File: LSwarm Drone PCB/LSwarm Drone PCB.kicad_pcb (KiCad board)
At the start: 4 copper layers, 100 x 99.8 mm, 135 parts, among them J1 Conn_01x04_Pin, J3 JST / BT2.0 Connector, J4 Conn_01x02_Pin, J5 Conn_01x02_Pin, J6 Conn_01x02_Pin, J7 Conn_01x02_Pin, Q1 AO3400A, Q2 AO3400A, Q3 AO3400A, Q4 AO3400A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

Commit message: sync
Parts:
- moved C59 2.50 mm to (54.5, 41.5)
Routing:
- net +3.3V: track 227.7 -> 230.4 mm
- net BATT_SW+: track 346.7 -> 344.4 mm

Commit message: sync
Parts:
- L6: value L -> 24nH
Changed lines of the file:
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@@
 		(capping no)
 		(filling no)
-		(zone_defaults)
 		(pcbplotparams
 			(layerselection 0x00000000_00000000_55555555_5755f5ff)
@@
 			)
 		)
-		(property "Value" "L"
+		(property "Value" "24nH"
 			(at 0 1.55 0)
 			(layer "F.Fab")

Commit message: sync
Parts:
- removed C52, C55: 12pF, Capacitor_SMD:C_0603_1608Metric
- removed C72: 220uF, Capacitor_Tantalum_SMD:CP_EIA-3528-21_Kemet-B
- removed L6: 24nH, Inductor_SMD:L_0805_2012Metric
- removed R18: 110k, Resistor_SMD:R_0603_1608Metric
- removed Y1: 12MHz, Crystal:Crystal_SMD_3225-4Pin_3.2x2.5mm
- removed Y3: 40MHz, Crystal:Crystal_SMD_3225-4Pin_3.2x2.5mm
- added C1: CL21A226MAQNNNE, easyeda2kicad:C0805, F.Cu at (54.0, 68.5)
- added R36: 820k, Resistor_SMD:R_0603_1608Metric, F.Cu at (62.5, 56.0)
- added R37: 100k, Resistor_SMD:R_0603_1608Metric, F.Cu at (66.0, 56.5)
- added X1: X322512MSB4SI, easyeda2kicad:CRYSTAL-SMD_4P-L3.2-W2.5-BL, F.Cu at (54.8, 52.3)
- R17: value 806k -> 10k
- moved R17 18.0 mm to (62.5, 74.0), turned to 0 degrees
- moved C7 4.72 mm to (56.5, 49.0), turned to -90 degrees
- moved C60 4.17 mm to (70.8, 40.0)
- moved C61 4.17 mm to (73.5, 36.5)
- moved L8 4.17 mm to (71.0, 38.5)
- moved JP1 3.76 mm to (73.5, 45.2)
- moved C8 1.11 mm to (55.0, 49.0), turned to -90 degrees
- renumbered C71C to C71Ceramic1
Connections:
- C7 pad 1: Net-(C7-Pad1) -> GND
- C7 pad 2: GND -> Net-(X1-OSC2)
- C8 pad 1: RP2350_XIN -> GND
- C8 pad 2: GND -> RP2350_XIN
- R17 pad 1: Net-(U3-FB) -> Net-(R17-Pad1)
- R17 pad 2: +5V -> Net-(Q7-G)
- R7 pad 1: Net-(C7-Pad1) -> Net-(X1-OSC2)
- SW1 pad 2: Net-(Q7-G) -> Net-(R17-Pad1)
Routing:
- net Net-(R17-Pad1): track 0.00 -> 51.4 mm, vias 0 -> 2
- net Net-(Q7-G): track 56.0 -> 9.82 mm, vias 3 -> 2
- net Net-(C7-Pad1): track 13.3 -> 0.00 mm, vias 2 -> 0
- net ESP32_40M_X0: track 12.4 -> 0.00 mm, vias 4 -> 0
- net Net-(C52-Pad1): track 10.1 -> 0.00 mm, vias 2 -> 0
- net Net-(ESP32-LNA_IN): track 22.9 -> 13.0 mm
- net Net-(X1-OSC2): track 0.00 -> 9.14 mm, vias 0 -> 2
- net ESP32_40M_X1: track 6.14 -> 0.00 mm
- net RP2350_XIN: track 20.7 -> 17.5 mm
- net GND: track 123.0 -> 125.4 mm, vias 102 -> 100
- net BATT_SW+: track 344.4 -> 342.4 mm
- net RP2350_GPIO_17: track 41.9 -> 40.2 mm
- net RP2350_GPIO_16: track 43.6 -> 42.8 mm
- net BATT+: track 16.3 -> 17.0 mm

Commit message: sync
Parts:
- added D5: USBLC6-2SC6_C2687116, easyeda2kicad:SOT-23-6_L2.9-W1.6-P0.95-LS2.8-BL, F.Cu at (50.0, 31.4)
- moved R32 12.5 mm to (56.5, 28.5)
- moved R33 10.5 mm to (46.0, 29.0)
- moved C60 7.32 mm to (63.5, 40.7), turned to 90 degrees
- moved C61 7.31 mm to (67.1, 40.0), turned to 90 degrees
- moved L8 6.23 mm to (65.3, 41.0)
- moved JP1 6.15 mm to (69.5, 40.6), turned to -90 degrees
- moved R35 5.49 mm to (45.2, 31.3), turned to 90 degrees
- moved R34 4.92 mm to (56.5, 30.5)
- moved C20 4.50 mm to (36.0, 59.7)
- moved C19 4.50 mm to (36.0, 56.5)
- moved C56 4.27 mm to (54.7, 41.0)
- moved C18 3.48 mm to (38.0, 56.5)
- moved C21 3.48 mm to (38.0, 59.7)
- moved C59 3.16 mm to (53.5, 44.5)
- moved C26 2.50 mm to (43.0, 25.0)
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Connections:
- R34 pad 1: Net-(USB1-DN1) -> Net-(D5-I/O2-Pad3)
- R35 pad 2: Net-(USB1-DP1) -> Net-(D5-I/O2-Pad4)
- USB1 pad A4: unconnected-(USB1-VBUS-PadA4) -> Net-(D5-VBUS)
- USB1 pad A9: unconnected-(USB1-VBUS-PadA4) -> Net-(D5-VBUS)
- USB1 pad B4: unconnected-(USB1-VBUS-PadA4) -> Net-(D5-VBUS)
- USB1 pad B9: unconnected-(USB1-VBUS-PadA4) -> Net-(D5-VBUS)
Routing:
- net Net-(D5-VBUS): track 0.00 -> 11.2 mm, vias 0 -> 2
- net RP2350_GPIO_22: track 36.8 -> 47.4 mm, vias 2 -> 4
- net Net-(USB1-DP1): track 16.8 -> 8.43 mm
- net Net-(JP1-SIG): track 10.8 -> 3.16 mm
- net Net-(USB1-DN1): track 15.3 -> 7.64 mm
- net RP2350_USB_DP: track 25.3 -> 17.8 mm
- net Net-(ESP32-LNA_IN): track 13.0 -> 5.46 mm
- net RP2350_GPIO_12: track 62.5 -> 55.7 mm, vias 7 -> 6
- net unconnected-(USB1-VBUS-PadA4): track 6.68 -> 0.00 mm
- net RP2350_USB_DM: track 27.5 -> 21.5 mm
- net GND: track 125.4 -> 131.2 mm, vias 100 -> 98
- net RP2350_GPIO_13: track 60.9 -> 55.2 mm, vias 5 -> 4
- net Net-(USB1-CC1): track 10.7 -> 6.16 mm, vias 2 -> 0
- net Net-(D5-I/O2-Pad3): track 0.00 -> 4.54 mm
- net Net-(RP2350-RUN): track 37.2 -> 32.9 mm
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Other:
- outline, holes or cut-outs redrawn

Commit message: sync
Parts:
- moved R34 3.89 mm to (52.8, 31.5), turned to -90 degrees
- moved R6 3.89 mm to (46.0, 36.1)
- moved R35 2.02 mm to (47.2, 31.7)
- turned C6 to 0 degrees
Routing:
- net RP2350_USB_DM: track 21.5 -> 16.9 mm, vias 2 -> 0
- net Net-(D5-I/O2-Pad3): track 4.54 -> 1.71 mm
- net Net-(RP2350-VREG_AVDD): track 24.7 -> 22.1 mm, vias 0 -> 2
- net +1V1: track 63.3 -> 61.4 mm
- net RP2350_USB_DP: track 17.8 -> 15.9 mm, vias 2 -> 0
- net Net-(D5-I/O2-Pad4): track 3.66 -> 1.85 mm
- net GND: track 131.2 -> 130.3 mm
- net +3.3V: track 232.9 -> 233.5 mm, vias 24 -> 26
- net RP2350_GPIO_24: track 25.9 -> 26.5 mm

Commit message: sync
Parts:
- removed J1: Conn_01x04_Pin, Connector_PinHeader_2.54mm:PinHeader_1x04_P2.54mm_Vertical
- added J2: Conn_01x06_Pin, Connector_PinHeader_2.54mm:PinHeader_1x06_P2.54mm_Vertical, F.Cu at (73.1, 44.6)
- added J8: Conn_01x05_Pin, Connector_PinHeader_2.54mm:PinHeader_1x05_P2.54mm_Vertical, F.Cu at (40.4, 64.0)
- moved C50 1.50 mm to (41.5, 70.0)
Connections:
- net Net-(RP2350-RUN) renamed RP2350_RUN
- net Net-(USB1-DN1) renamed USB_D-
- net Net-(USB1-DP1) renamed USB_D+
- net RP2350_USB_DM renamed RP2350_USB_DN
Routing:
- net RP2350_RUN: track 32.9 -> 42.5 mm, vias 3 -> 5
- net RP2350_GPIO_15: track 85.5 -> 94.4 mm, vias 9 -> 10
- net RP2350_GPIO_14: track 92.0 -> 99.5 mm, vias 5 -> 7
- net RP2350_GPIO_17: track 37.0 -> 42.4 mm
- net RP2350_GPIO_16: track 41.8 -> 46.9 mm
- net +3.3V: track 233.5 -> 237.4 mm, vias 26 -> 25
- net RP2350_QSPI_SD3: track 9.82 -> 12.7 mm
- net GND: track 130.3 -> 132.4 mm, vias 98 -> 99
- net RP2350_GPIO_20: track 43.5 -> 45.4 mm
- net RP2350_SWDIO: track 16.7 -> 18.3 mm
- net RP2350_SWCLK: track 19.4 -> 20.9 mm
- net RP2350_QSPI_SCLK: track 11.3 -> 12.6 mm
- net +5V: track 319.5 -> 320.4 mm
- net RP2350_USB_DN: track 16.9 -> 16.1 mm
- net RP2350_GPIO_13: track 55.2 -> 55.8 mm
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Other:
- board text added: "3.3+"
- board text added: "BOOT"
- board text added: "CLK"
- board text added: "DIO"
- board text added: "EN"
- board text added: "GND"
- board text added: "RUN"
- board text added: "RX"
- board text added: "TX"

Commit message: sync
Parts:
- removed C26: 10nF, Capacitor_SMD:C_0603_1608Metric
- removed D5: USBLC6-2SC6_C2687116, easyeda2kicad:SOT-23-6_L2.9-W1.6-P0.95-LS2.8-BL
- removed R32, R33: 5.1k, Resistor_SMD:R_0603_1608Metric
- removed R34, R35: 27, Resistor_SMD:R_0603_1608Metric
- removed USB1: USB-TYPE-C-018, easyeda2kicad:USB-C_SMD-TYPE-C-31-M-12
- added C27: 10nF, Capacitor_SMD:C_0603_1608Metric, F.Cu at (43.0, 25.0)
- added D6: USBLC6-2SC6_C2687116, easyeda2kicad:SOT-23-6_L2.9-W1.6-P0.95-LS2.8-BL, F.Cu at (50.3, 31.2)
- added R38: 5.1k, Resistor_SMD:R_0603_1608Metric, F.Cu at (44.0, 29.0)
- added R39: 27, Resistor_SMD:R_0603_1608Metric, F.Cu at (47.5, 32.0)
- added R40: 27, Resistor_SMD:R_0603_1608Metric, F.Cu at (53.0, 31.6)
- added R41: 5.1k, Resistor_SMD:R_0603_1608Metric, F.Cu at (55.2, 29.0)
- added USB2: USB-TYPE-C-018, easyeda2kicad:USB-C_SMD-TYPE-C-31-M-12, F.Cu at (50.2, 25.0)
- moved C3 0.21 mm to (52.9, 36.0)
- moved C6 0.21 mm to (53.0, 34.2)
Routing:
- net Net-(C27-Pad2): track 0.00 -> 19.3 mm
- net Net-(C26-Pad2): track 19.3 -> 0.00 mm
- net USB_VBUS: track 0.00 -> 15.9 mm, vias 0 -> 2
- net Net-(D5-VBUS): track 11.2 -> 0.00 mm, vias 2 -> 0
- net Net-(USB2-CC2): track 0.00 -> 7.95 mm
- net Net-(USB2-CC1): track 0.00 -> 6.28 mm
- net Net-(USB1-CC1): track 6.16 -> 0.00 mm
- net Net-(USB1-CC2): track 5.95 -> 0.00 mm
- net USB_D+: track 8.64 -> 5.55 mm
- net GND: track 132.4 -> 134.9 mm, vias 99 -> 98
- net Net-(D6-I/O1-Pad6): track 0.00 -> 2.46 mm
- net Net-(D6-I/O2-Pad4): track 0.00 -> 2.44 mm
- net Net-(D5-I/O2-Pad4): track 1.85 -> 0.00 mm
- net Net-(D5-I/O2-Pad3): track 1.71 -> 0.00 mm
- net USB_D-: track 7.25 -> 5.61 mm

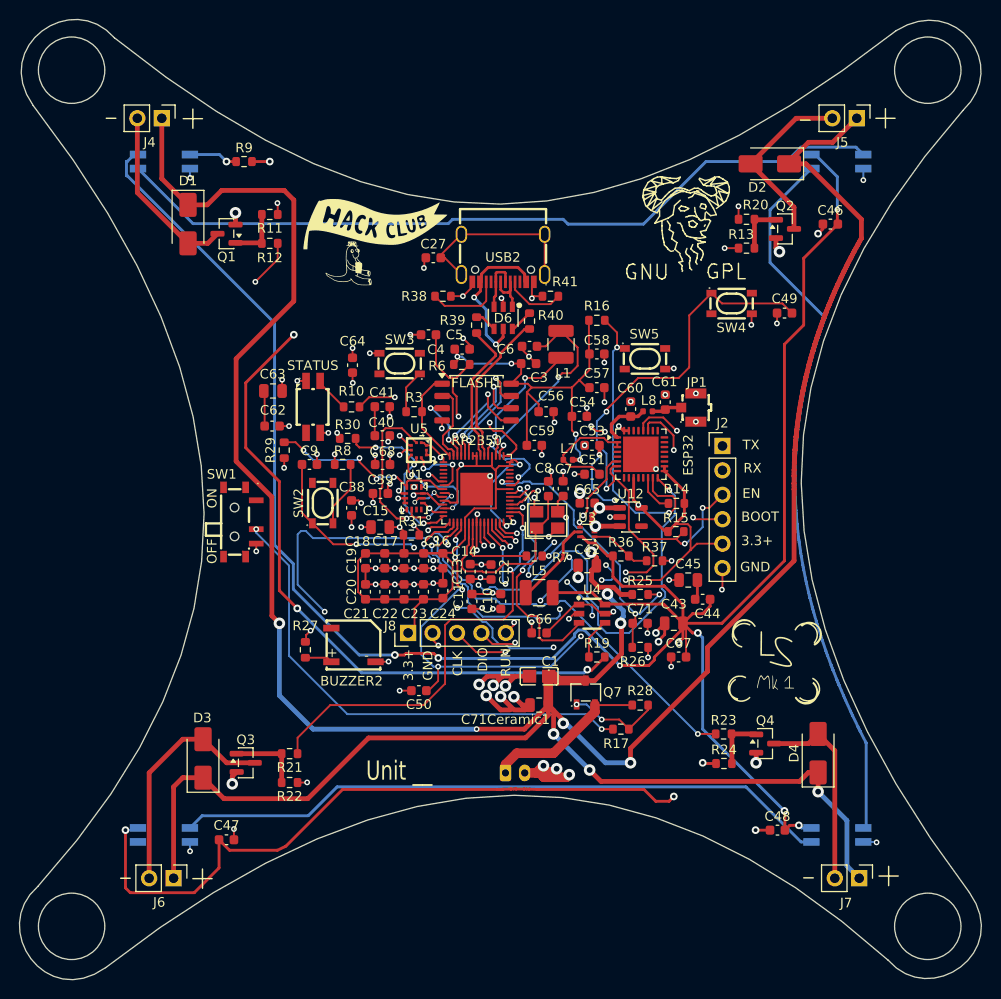
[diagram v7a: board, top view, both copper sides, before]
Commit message: finished new pcb wiring
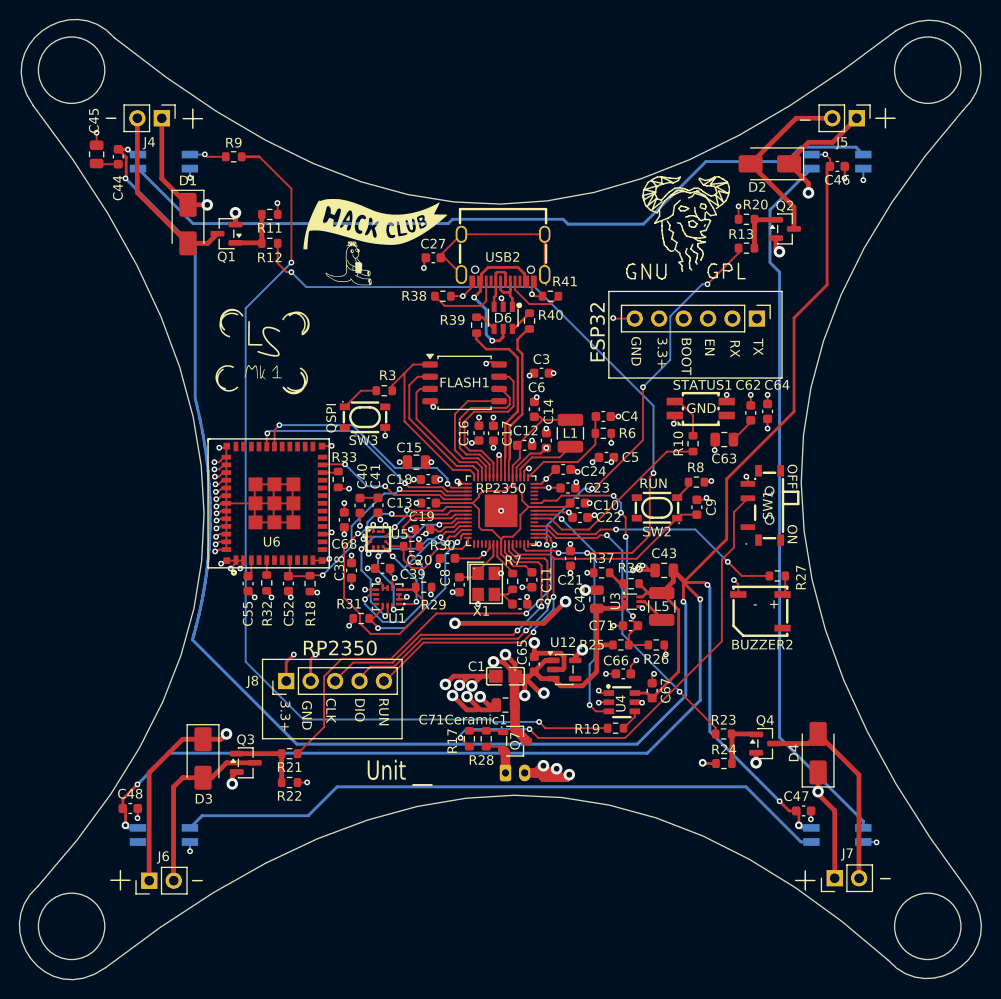
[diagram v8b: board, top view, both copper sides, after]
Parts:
- removed C49, C50, C51, C53, C56, C57, C58: 100nF, Capacitor_SMD:C_0603_1608Metric
- removed C54: 10nF, Capacitor_SMD:C_0603_1608Metric
- removed C59: 1uF, Capacitor_SMD:C_0603_1608Metric
- removed C60, C61: 3.3pF, Capacitor_SMD:C_0603_1608Metric
- removed ESP32: ESP32-C3, Package_DFN_QFN:QFN-32-1EP_5x5mm_P0.5mm_EP3.7x3.7mm
- removed JP1: U.FL-R-SMT-1, easyeda2kicad:RF-SMD_FRF05002-JSS103M
- removed L7: 2nH, Inductor_SMD:L_0402_1005Metric
- removed L8: 2.2nH, Inductor_SMD:L_0402_1005Metric
- removed R14, R15, R16: 10k, Resistor_SMD:R_0603_1608Metric
- removed SW4, SW5: SKRPACE010, easyeda2kicad:KEY-SMD_4P-L4.2-W3.2-P2.20-LS4.6
- added C52: 1uF, Capacitor_SMD:C_0603_1608Metric, F.Cu at (27.9, 58.9)
- added C55: 10uF, Capacitor_SMD:C_0603_1608Metric, F.Cu at (23.7, 58.9)
- added R18: 10k, Resistor_SMD:R_0603_1608Metric, F.Cu at (30.2, 58.9)
- added R32: 10k, Resistor_SMD:R_0603_1608Metric, F.Cu at (25.7, 58.8)
- added R33: 10k, Resistor_SMD:R_0603_1608Metric, F.Cu at (33.1, 48.0)
- added U6: ESP32-C3-MINI-1U-N4, easyeda2kicad:WIFIM-SMD_61P-L13.2-W12.5-P0.80, F.Cu at (26.5, 50.5)
- C7, C8: value 15pF -> 33pF
- moved C44 76.2 mm to (10.2, 14.5), turned to 90 degrees
- moved C45 75.8 mm to (8.00, 14.2), turned to -90 degrees
- moved C48 67.3 mm to (11.5, 82.2), turned to 180 degrees
- moved logo 62.3 mm to (21.6, 35.6)
- moved C47 60.1 mm to (81.5, 82.5)
- moved SW1 54.5 mm to (77.4, 50.8), turned to 90 degrees
- moved C62 49.8 mm to (76.0, 41.1), turned to 90 degrees
- moved R27 49.7 mm to (78.8, 58.1), turned to 0 degrees
- moved C63 47.2 mm to (73.2, 43.9), turned to 0 degrees
- moved C64 43.4 mm to (77.8, 41.0), turned to 90 degrees
- moved BUZZER2 42.4 mm to (77.0, 61.8), turned to 180 degrees
- moved C9 40.5 mm to (70.4, 50.9), turned to 90 degrees
- moved STATUS1 40.3 mm to (70.8, 40.7), turned to 0 degrees
- moved R8 36.8 mm to (70.3, 48.3), turned to 180 degrees
- moved R10 35.7 mm to (70.0, 44.3), turned to -90 degrees
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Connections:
- C8 pad 1: GND -> RP2350_XIN
- C8 pad 2: RP2350_XIN -> GND
- R7 pad 1: Net-(X1-OSC2) -> RP2350_XOUT
- R7 pad 2: RP2350_XOUT -> Net-(X1-OSC2)
- RP2350 pad 16: RP2350_GPIO_12 -> unconnected-(RP2350-GPIO12-Pad16)
- RP2350 pad 17: RP2350_GPIO_13 -> unconnected-(RP2350-GPIO13-Pad17)
- RP2350 pad 18: RP2350_GPIO_14 -> unconnected-(RP2350-GPIO14-Pad18)
- RP2350 pad 19: RP2350_GPIO_15 -> unconnected-(RP2350-GPIO15-Pad19)
- RP2350 pad 27: RP2350_GPIO_16 -> unconnected-(RP2350-GPIO16-Pad27)
- RP2350 pad 28: RP2350_GPIO_17 -> unconnected-(RP2350-GPIO17-Pad28)
- RP2350 pad 41: RP2350_GPIO_27_ADC -> unconnected-(RP2350-GPIO27/ADC1-Pad41)
- RP2350 pad 42: RP2350_GPIO_28_ADC -> unconnected-(RP2350-GPIO28/ADC2-Pad42)
- RP2350 pad 43: RP2350_GPIO_29_ADC -> unconnected-(RP2350-GPIO29/ADC3-Pad43)
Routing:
- net +3.3V: track 237.3 -> 63.7 mm, vias 25 -> 39
- net RP2350_GPIO_14: track 99.5 -> 0.00 mm, vias 7 -> 0
- net RP2350_GPIO_15: track 94.4 -> 0.00 mm, vias 10 -> 0
- net RP2350_GPIO_13: track 55.8 -> 0.00 mm, vias 4 -> 0
- net RP2350_GPIO_12: track 55.2 -> 0.00 mm, vias 6 -> 0
- net GND: track 134.9 -> 189.0 mm, vias 98 -> 109
- net RP2350_GPIO_16: track 46.9 -> 0.00 mm, vias 4 -> 0
- net RP2350_GPIO_17: track 42.4 -> 0.00 mm, vias 4 -> 0
- net BATT_SW+: track 342.4 -> 313.9 mm, vias 12 -> 8
- net RP2350_GPIO_2: track 0.00 -> 25.6 mm, vias 0 -> 2
- net RP2350_GPIO_0: track 0.00 -> 25.1 mm, vias 0 -> 2
- net RP2350_GPIO_1: track 0.00 -> 25.0 mm, vias 0 -> 2
- net RP2350_GPIO_22: track 47.4 -> 27.0 mm, vias 4 -> 2
- net RP2350_GPIO_6: track 6.72 -> 25.4 mm
- net RP2350_GPIO_21: track 52.0 -> 33.5 mm, vias 3 -> 2
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- added copper zone on In2.Cu, net +3.3V
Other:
- board text added: "ESP32"
- board text added: "QSPI"
- board text added: "RP2350"
